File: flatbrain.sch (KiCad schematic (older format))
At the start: 107 parts, among them J1 OLED, SW41 Rotary_Encoder_Switch, SW42 Rotary_Encoder_Switch, U1 Elite-C

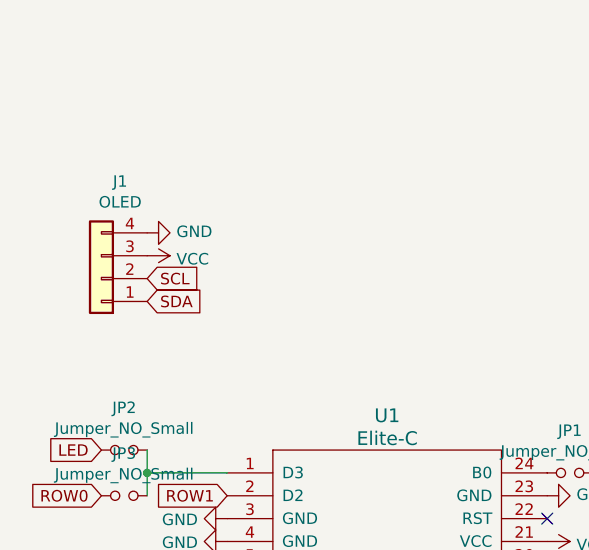
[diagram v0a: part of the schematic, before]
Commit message: reverse oled pins
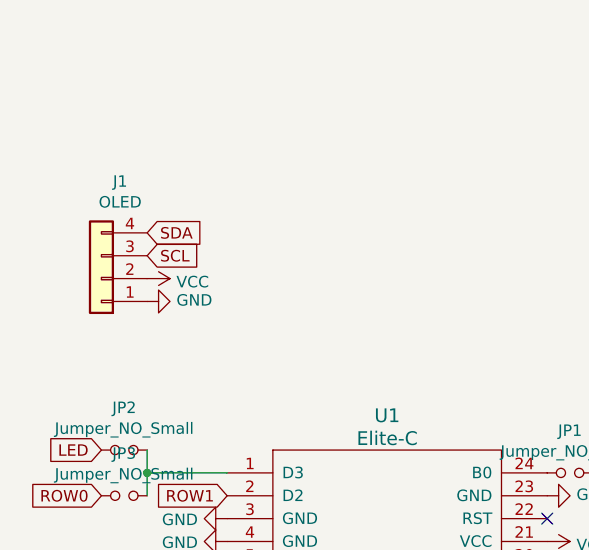
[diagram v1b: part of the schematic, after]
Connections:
- net GND: now also J1.1 (Pin_1); no longer J1.4 (Pin_4)
- net SCL: now also J1.3 (Pin_3); no longer J1.2 (Pin_2)
- net SDA: now also J1.4 (Pin_4); no longer J1.1 (Pin_1)
- net VCC: now also J1.2 (Pin_2); no longer J1.3 (Pin_3)
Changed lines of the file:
@@
 L power:GND #PWR0105
 U 1 1 5F13EA26
-P 1100 1450
-F 0 "#PWR0105" H 1100 1200 50  0001 C CNN
-F 1 "GND" V 1105 1322 50  0000 R CNN
-F 2 "" H 1100 1450 50  0001 C CNN
-F 3 "" H 1100 1450 50  0001 C CNN
-	1    1100 1450
+P 1100 1750
+F 0 "#PWR0105" H 1100 1500 50  0001 C CNN
+F 1 "GND" V 1105 1622 50  0000 R CNN
+F 2 "" H 1100 1750 50  0001 C CNN
+F 3 "" H 1100 1750 50  0001 C CNN
+	1    1100 1750
 	0    -1   -1   0
 $EndComp
@@
 L power:VCC #PWR0106
 U 1 1 5F13F1C5
-P 1100 1550
-F 0 "#PWR0106" H 1100 1400 50  0001 C CNN
-F 1 "VCC" V 1115 1678 50  0000 L CNN
-F 2 "" H 1100 1550 50  0001 C CNN
-F 3 "" H 1100 1550 50  0001 C CNN
-	1    1100 1550
+P 1100 1650
+F 0 "#PWR0106" H 1100 1500 50  0001 C CNN
+F 1 "VCC" V 1115 1778 50  0000 L CNN
+F 2 "" H 1100 1650 50  0001 C CNN
+F 3 "" H 1100 1650 50  0001 C CNN
+	1    1100 1650
 	0    1    1    0
 $EndComp
-Text GLabel 1100 1650 2    50   Input ~ 0
+Text GLabel 1100 1550 2    50   Input ~ 0
 SCL
-Text GLabel 1100 1750 2    50   Input ~ 0
+Text GLabel 1100 1450 2    50   Input ~ 0
 SDA
 Text GLabel 1450 2900 0    50   Input ~ 0
